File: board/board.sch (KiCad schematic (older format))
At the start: 22 parts, among them CON1 NRF24L01+MODULE, CON2 AVR-ISP-6, IC1 ATMEGA88PA-A, SW1 SW_PUSH, U1 XR1151

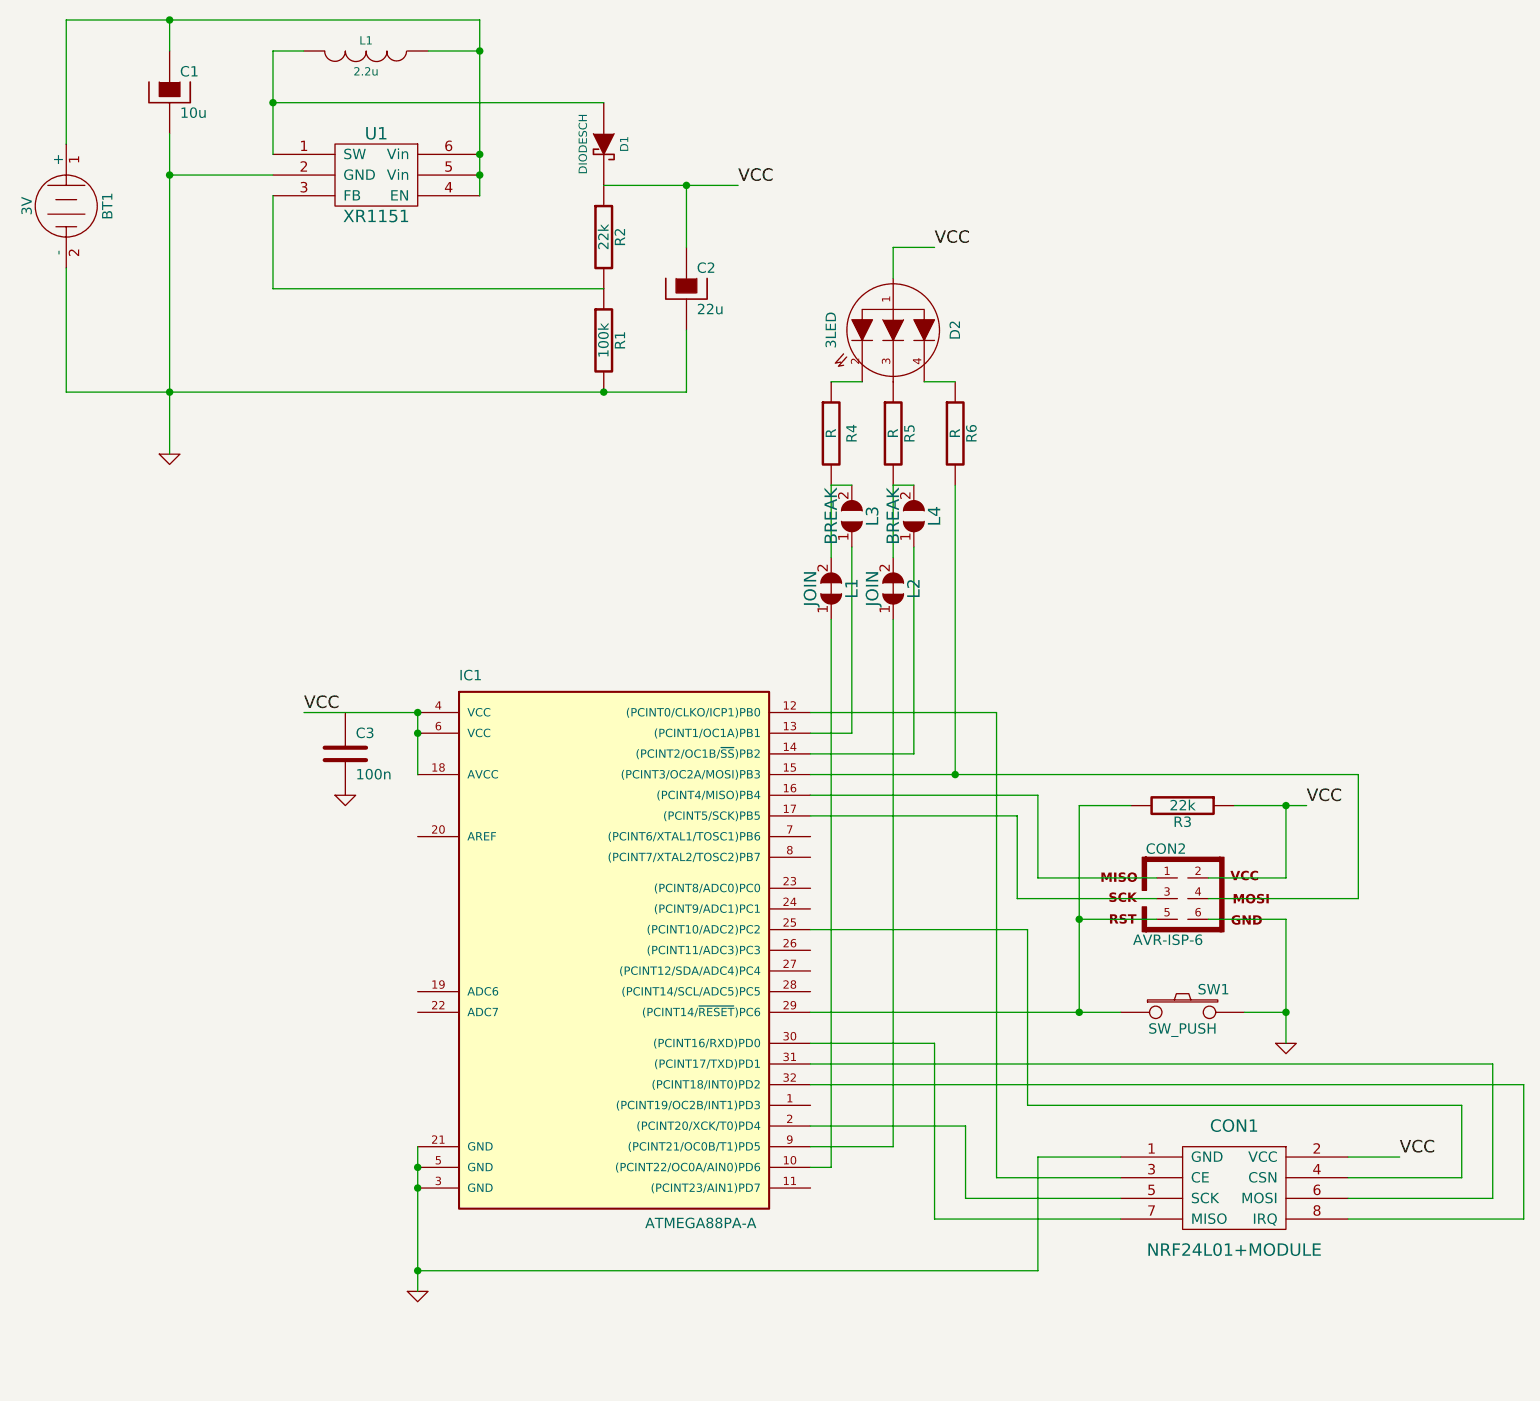
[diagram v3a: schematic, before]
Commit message: Add debug port
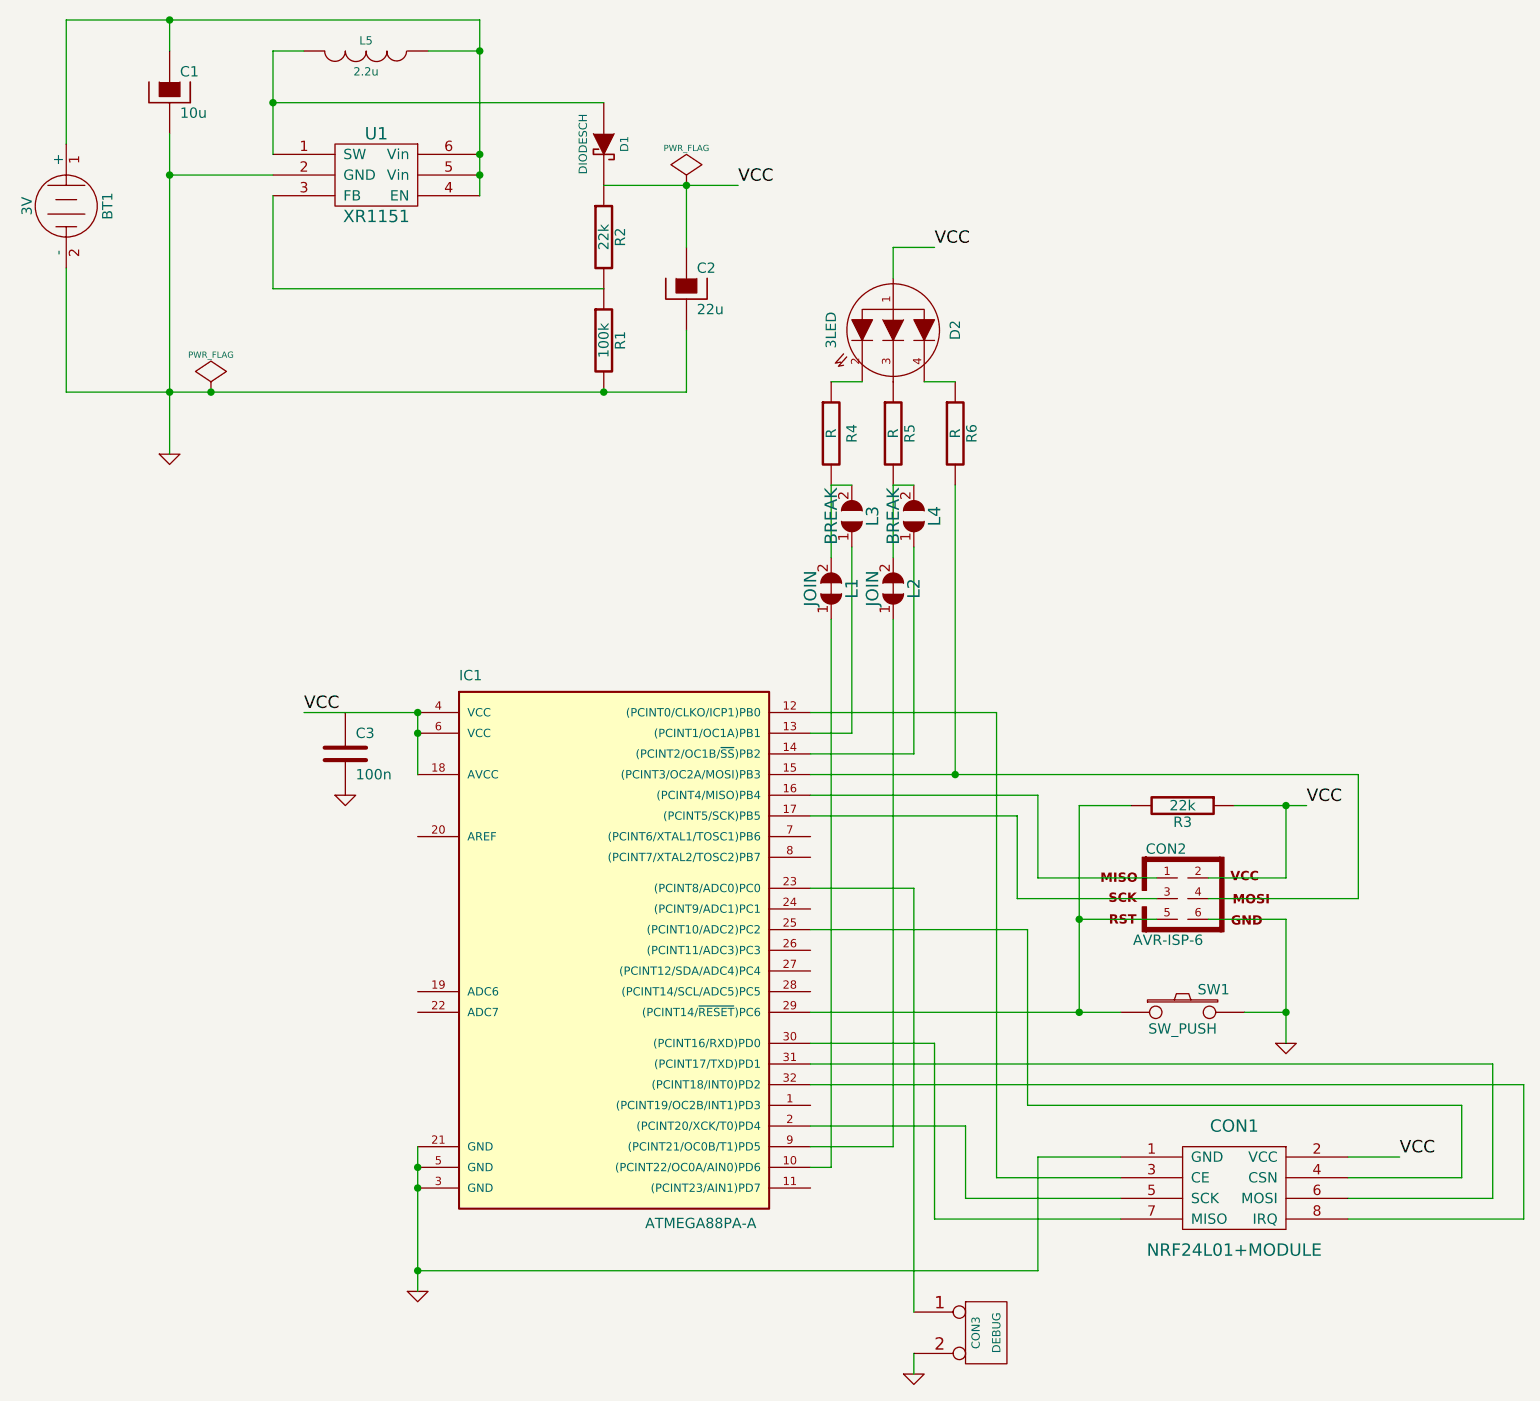
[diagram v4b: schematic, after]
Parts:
- added CON3: DEBUG, symbol CONN_2
- renumbered L1 to L5
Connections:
- net GND: now also CON3.2 (PM)
- net at IC1.23 ((PCINT8/ADC0)PC0): now also CON3.1 (P1)
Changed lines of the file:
@@
-EESchema Schematic File Version 2  date Thu 27 Mar 2014 20:11:46 CST
+EESchema Schematic File Version 2  date Thu 27 Mar 2014 20:33:20 CST
 LIBS:power
 LIBS:device
@@
 Comment4 ""
 $EndDescr
-Wire Wire Line
-	5000 3700 5000 3350
-Wire Wire Line
-	4700 4000 4700 6650
+Connection ~ 1700 2900
+$Comp
+L PWR_FLAG #FLG01
+U 1 1 5333F6A5
+P 1700 2900
+F 0 "#FLG01" H 1700 2995 30  0001 C CNN
+F 1 "PWR_FLAG" H 1700 3080 30  0000 C CNN
+	1    1700 2900
+	1    0    0    -1
+$EndComp
+$Comp
+L PWR_FLAG #FLG02
+U 1 1 5333F69A
+P 4000 1900
+F 0 "#FLG02" H 4000 1995 30  0001 C CNN
+F 1 "PWR_FLAG" H 4000 2080 30  0000 C CNN
+	1    4000 1900
+	1    0    0    -1
+$EndComp
+Wire Wire Line
+	5100 7550 5100 7650
+Wire Wire Line
+	5100 7350 5100 5300
+Wire Wire Line
+	5100 5300 4600 5300
+Wire Wire Line
+	5000 4000 5000 6550
+Wire Wire Line
+	4700 3700 4700 3350
+Wire Wire Line
+	5200 2200 5000 2200
+Wire Wire Line
+	5000 2200 5000 2350
+Wire Wire Line
+	4850 2850 4700 2850
+Wire Wire Line
+	4700 3350 4800 3350
+Wire Wire Line
+	7200 6700 7750 6700
+Wire Wire Line
+	1000 1100 3000 1100
+Wire Wire Line
+	1000 2900 4000 2900
+Wire Wire Line
+	1000 2900 1000 2300
+Connection ~ 5900 5900
+Wire Wire Line
+	4600 5900 6100 5900
+Wire Wire Line
+	6525 5350 7250 5350
+Wire Wire Line
+	7250 5350 7250 4750
+Wire Wire Line
+	6900 6050 6900 5450
+Wire Wire Line
+	6900 5450 6525 5450
+Wire Wire Line
+	5900 5900 5900 4900
+Wire Wire Line
+	6900 4900 6900 5250
+Wire Wire Line
+	6275 5250 5700 5250
+Connection ~ 5300 4750
+Wire Wire Line
+	7250 4750 4600 4750
+Wire Wire Line
+	7200 6900 8050 6900
+Wire Wire Line
+	8050 6900 8050 6250
+Wire Wire Line
+	8050 6250 4600 6250
+Wire Wire Line
+	5000 6550 4600 6550
+Wire Wire Line
+	6100 6600 5700 6600
+Wire Wire Line
+	5700 6600 5700 7150
+Connection ~ 2700 7150
+Wire Wire Line
+	5700 7150 2700 7150
+Wire Wire Line
+	4600 4450 5500 4450
+Wire Wire Line
+	5500 4450 5500 6700
+Wire Wire Line
+	5500 6700 6100 6700
+Wire Wire Line
+	4600 6050 5200 6050
+Wire Wire Line
+	5200 6050 5200 6900
+Wire Wire Line
+	5200 6900 6100 6900
+Connection ~ 2700 4450
+Connection ~ 2700 6650
+Wire Wire Line
+	2700 6550 2700 7250
+Connection ~ 3600 2900
+Wire Wire Line
+	4000 2900 4000 2600
+Connection ~ 1500 2900
+Wire Wire Line
+	1500 1250 1500 1100
+Wire Wire Line
+	2000 1750 2000 1250
+Wire Wire Line
+	2000 1250 2150 1250
+Wire Wire Line
+	2000 1950 2000 2400
+Wire Wire Line
+	2000 2400 3600 2400
+Connection ~ 3000 1750
+Connection ~ 3000 1850
+Wire Wire Line
+	2000 1850 1500 1850
+Connection ~ 3000 1250
+Wire Wire Line
+	2750 1250 3000 1250
+Wire Wire Line
+	3600 1500 2000 1500
+Connection ~ 2000 1500
+Wire Wire Line
+	1500 1650 1500 3200
+Connection ~ 1500 1850
+Wire Wire Line
+	4000 2200 4000 1900
+Wire Wire Line
+	2150 4450 2700 4450
+Wire Wire Line
+	4250 1900 3600 1900
+Connection ~ 4000 1900
+Connection ~ 2700 6750
+Wire Wire Line
+	6100 6800 5350 6800
+Wire Wire Line
+	5350 6800 5350 6450
+Wire Wire Line
+	5350 6450 4600 6450
+Wire Wire Line
+	4600 6650 4700 6650
+Wire Wire Line
+	5300 3350 5300 4750
+Wire Wire Line
+	7200 6600 7450 6600
+Wire Wire Line
+	4600 6150 7900 6150
+Wire Wire Line
+	7900 6150 7900 6800
+Wire Wire Line
+	7900 6800 7200 6800
+Wire Wire Line
+	5700 5250 5700 4850
+Wire Wire Line
+	5700 4850 4600 4850
+Wire Wire Line
+	6900 5250 6525 5250
+Wire Wire Line
+	4600 4950 5600 4950
+Wire Wire Line
+	5600 4950 5600 5350
+Wire Wire Line
+	5600 5350 6275 5350
+Wire Wire Line
+	5900 4900 6150 4900
+Wire Wire Line
+	6275 5450 5900 5450
+Connection ~ 5900 5450
+Wire Wire Line
+	6650 4900 7000 4900
+Connection ~ 6900 4900
+Wire Wire Line
+	6700 5900 6900 5900
+Connection ~ 6900 5900
+Wire Wire Line
+	1000 1100 1000 1700
+Connection ~ 1500 1100
+Wire Wire Line
+	3000 1100 3000 1950
+Wire Wire Line
+	2700 4450 2700 4750
+Connection ~ 2700 4550
+Wire Wire Line
+	7750 6700 7750 6350
+Wire Wire Line
+	7750 6350 5650 6350
+Wire Wire Line
+	5650 6350 5650 5500
+Wire Wire Line
+	5650 5500 4600 5500
+Wire Wire Line
+	4600 4550 4800 4550
+Wire Wire Line
+	4800 4550 4800 3650
+Wire Wire Line
+	5100 3350 5000 3350
+Wire Wire Line
+	5100 3650 5100 4650
+Wire Wire Line
+	5100 4650 4600 4650
 Wire Wire Line
 	5150 2850 5300 2850
 Wire Wire Line
-	4600 4650 5100 4650
-Wire Wire Line
-	5100 4650 5100 3650
-Wire Wire Line
-	5000 3350 5100 3350
-Wire Wire Line
-	4800 3650 4800 4550
-Wire Wire Line
-	4800 4550 4600 4550
-Wire Wire Line
-	4600 5500 5650 5500
-Wire Wire Line
-	5650 5500 5650 6350
-Wire Wire Line
-	5650 6350 7750 6350
-Wire Wire Line
-	7750 6350 7750 6700
-Connection ~ 2700 4550
-Wire Wire Line
-	2700 4750 2700 4450
-Wire Wire Line
-	3000 1950 3000 1100
-Connection ~ 1500 1100
-Wire Wire Line
-	1000 1700 1000 1100
-Connection ~ 6900 5900
-Wire Wire Line
-	6700 5900 6900 5900
-Connection ~ 6900 4900
-Wire Wire Line
-	6650 4900 7000 4900
-Connection ~ 5900 5450
-Wire Wire Line
-	6275 5450 5900 5450
-Wire Wire Line
-	6150 4900 5900 4900
-Wire Wire Line
-	6275 5350 5600 5350
-Wire Wire Line
-	5600 5350 5600 4950
-Wire Wire Line
-	5600 4950 4600 4950
-Wire Wire Line
-	6525 5250 6900 5250
-Wire Wire Line
-	4600 4850 5700 4850
-Wire Wire Line
-	5700 4850 5700 5250
-Wire Wire Line
-	7200 6800 7900 6800
-Wire Wire Line
-	7900 6800 7900 6150
-Wire Wire Line
-	7900 6150 4600 6150
-Wire Wire Line
-	7200 6600 7450 6600
-Wire Wire Line
-	5300 3350 5300 4750
-Wire Wire Line
-	4700 6650 4600 6650
-Wire Wire Line
-	4600 6450 5350 6450
-Wire Wire Line
-	5350 6450 5350 6800
-Wire Wire Line
-	5350 6800 6100 6800
-Connection ~ 2700 6750
-Connection ~ 4000 1900
-Wire Wire Line
-	4250 1900 3600 1900
-Wire Wire Line
-	2700 4450 2150 4450
-Wire Wire Line
-	4000 2200 4000 1900
-Connection ~ 1500 1850
-Wire Wire Line
-	1500 1650 1500 3200
-Connection ~ 2000 1500
-Wire Wire Line
-	3600 1500 2000 1500
-Wire Wire Line
-	2750 1250 3000 1250
-Connection ~ 3000 1250
-Wire Wire Line
-	2000 1850 1500 1850
-Connection ~ 3000 1850
-Connection ~ 3000 1750
-Wire Wire Line
-	3600 2400 2000 2400
-Wire Wire Line
-	2000 2400 2000 1950
-Wire Wire Line
-	2150 1250 2000 1250
-Wire Wire Line
-	2000 1250 2000 1750
-Wire Wire Line
-	1500 1250 1500 1100
-Connection ~ 1500 2900
-Wire Wire Line
-	4000 2600 4000 2900
-Connection ~ 3600 2900
-Wire Wire Line
-	2700 6550 2700 7250
-Connection ~ 2700 6650
-Connection ~ 2700 4450
-Wire Wire Line
-	6100 6900 5200 6900
-Wire Wire Line
-	5200 6900 5200 6050
-Wire Wire Line
-	5200 6050 4600 6050
-Wire Wire Line
-	6100 6700 5500 6700
-Wire Wire Line
-	5500 6700 5500 4450
-Wire Wire Line
-	5500 4450 4600 4450
-Wire Wire Line
-	2700 7150 5700 7150
-Connection ~ 2700 7150
-Wire Wire Line
-	5700 7150 5700 6600
-Wire Wire Line
-	5700 6600 6100 6600
-Wire Wire Line
-	4600 6550 5000 6550
-Wire Wire Line
-	4600 6250 8050 6250
-Wire Wire Line
-	8050 6250 8050 6900
-Wire Wire Line
-	8050 6900 7200 6900
-Wire Wire Line
-	4600 4750 7250 4750
-Connection ~ 5300 4750
-Wire Wire Line
-	5700 5250 6275 5250
-Wire Wire Line
-	6900 5250 6900 4900
-Wire Wire Line
-	5900 4900 5900 5900
-Wire Wire Line
-	6525 5450 6900 5450
-Wire Wire Line
-	6900 5450 6900 6050
-Wire Wire Line
-	7250 4750 7250 5350
-Wire Wire Line
-	7250 5350 6525 5350
-Wire Wire Line
-	4600 5900 6100 5900
-Connection ~ 5900 5900
-Wire Wire Line
-	1000 2300 1000 2900
-Wire Wire Line
-	1000 2900 4000 2900
-Wire Wire Line
-	1000 1100 3000 1100
-Wire Wire Line
-	7750 6700 7200 6700
-Wire Wire Line
-	4800 3350 4700 3350
-Wire Wire Line
-	4850 2850 4700 2850
-Wire Wire Line
-	5000 2350 5000 2200
-Wire Wire Line
-	5000 2200 5200 2200
-Wire Wire Line
-	4700 3350 4700 3700
-Wire Wire Line
-	5000 6550 5000 4000
+	4700 6650 4700 4000
+Wire Wire Line
+	5000 3350 5000 3700
+$Comp
+L GND #PWR03
+U 1 1 5333F33C
+P 5100 7650
+F 0 "#PWR03" H 5100 7650 30  0001 C CNN
+F 1 "GND" H 5100 7580 30  0001 C CNN
+	1    5100 7650
+	1    0    0    -1
+$EndComp
+$Comp
+L CONN_2 CON3
+U 1 1 5333F2CA
+P 5450 7450
+F 0 "CON3" V 5400 7450 40  0000 C CNN
+F 1 "DEBUG" V 5500 7450 40  0000 C CNN
+	1    5450 7450
+	1    0    0    -1
+$EndComp
 $Comp
 L JOIN L2
@@
 $EndComp
 $Comp
-L GND #PWR?
+L GND #PWR04
 U 1 1 532E9E6A
 P 2350 4850
-F 0 "#PWR?" H 2350 4850 30  0001 C CNN
+F 0 "#PWR04" H 2350 4850 30  0001 C CNN
 F 1 "GND" H 2350 4780 30  0001 C CNN
 	1    2350 4850
@@
 $EndComp
 $Comp
-L GND #PWR?
+L GND #PWR05
 U 1 1 532E9CA2
 P 6900 6050
-F 0 "#PWR?" H 6900 6050 30  0001 C CNN
+F 0 "#PWR05" H 6900 6050 30  0001 C CNN
 F 1 "GND" H 6900 5980 30  0001 C CNN
 	1    6900 6050
@@
 $EndComp
 $Comp
-L GND #PWR?
+L GND #PWR06
 U 1 1 532D2506
 P 2700 7250
-F 0 "#PWR?" H 2700 7250 30  0001 C CNN
+F 0 "#PWR06" H 2700 7250 30  0001 C CNN
 F 1 "GND" H 2700 7180 30  0001 C CNN
 	1    2700 7250
@@
 $EndComp
 $Comp
-L INDUCTOR L1
+L INDUCTOR L5
 U 1 1 532D2091
 P 2450 1250
-F 0 "L1" V 2400 1250 40  0000 C CNN
+F 0 "L5" V 2400 1250 40  0000 C CNN
 F 1 "2.2u" V 2550 1250 40  0000 C CNN
 	1    2450 1250
@@
 $EndComp
 $Comp
-L GND #PWR?
+L GND #PWR07
 U 1 1 532D2016
 P 1500 3200
-F 0 "#PWR?" H 1500 3200 30  0001 C CNN
+F 0 "#PWR07" H 1500 3200 30  0001 C CNN
 F 1 "GND" H 1500 3130 30  0001 C CNN
 	1    1500 3200
